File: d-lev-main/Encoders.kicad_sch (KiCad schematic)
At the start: 8 parts, among them SW1 RotaryEncoder_Switch, SW2 RotaryEncoder_Switch, SW3 RotaryEncoder_Switch, SW4 RotaryEncoder_Switch, SW5 RotaryEncoder_Switch, SW6 RotaryEncoder_Switch, SW7 RotaryEncoder_Switch, SW8 RotaryEncoder_Switch

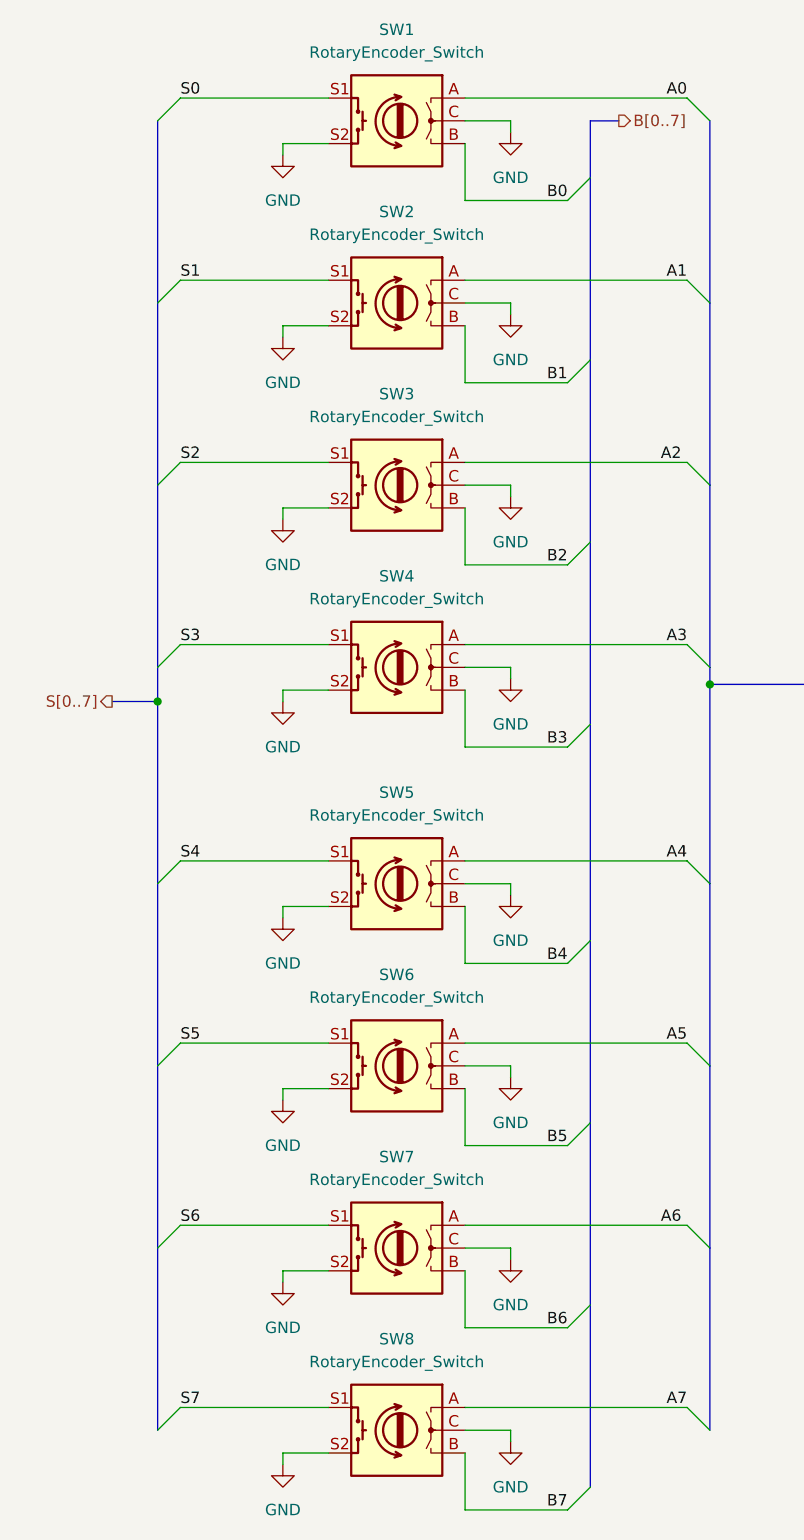
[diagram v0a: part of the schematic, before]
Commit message: Add block diagram
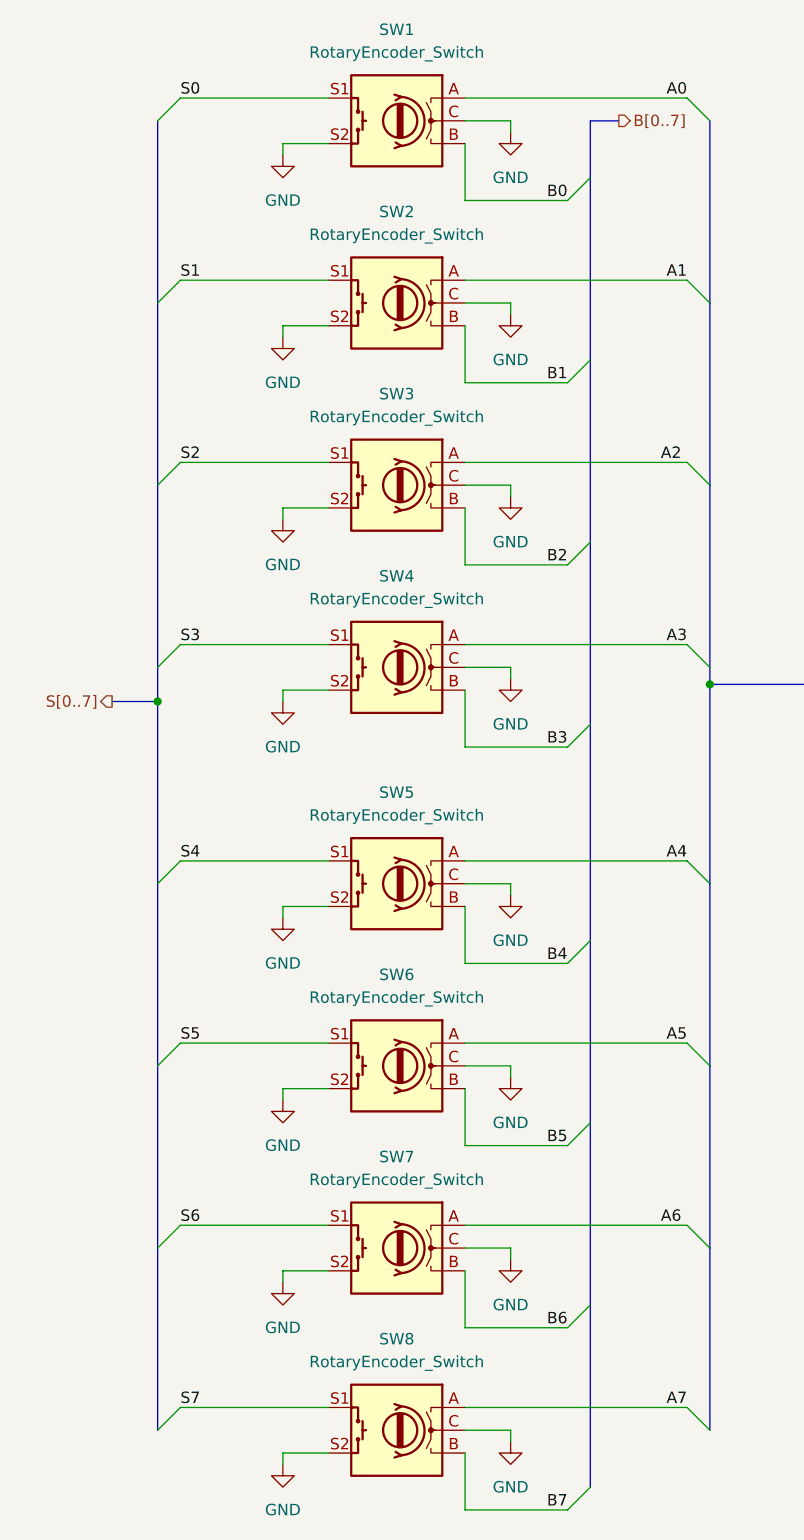
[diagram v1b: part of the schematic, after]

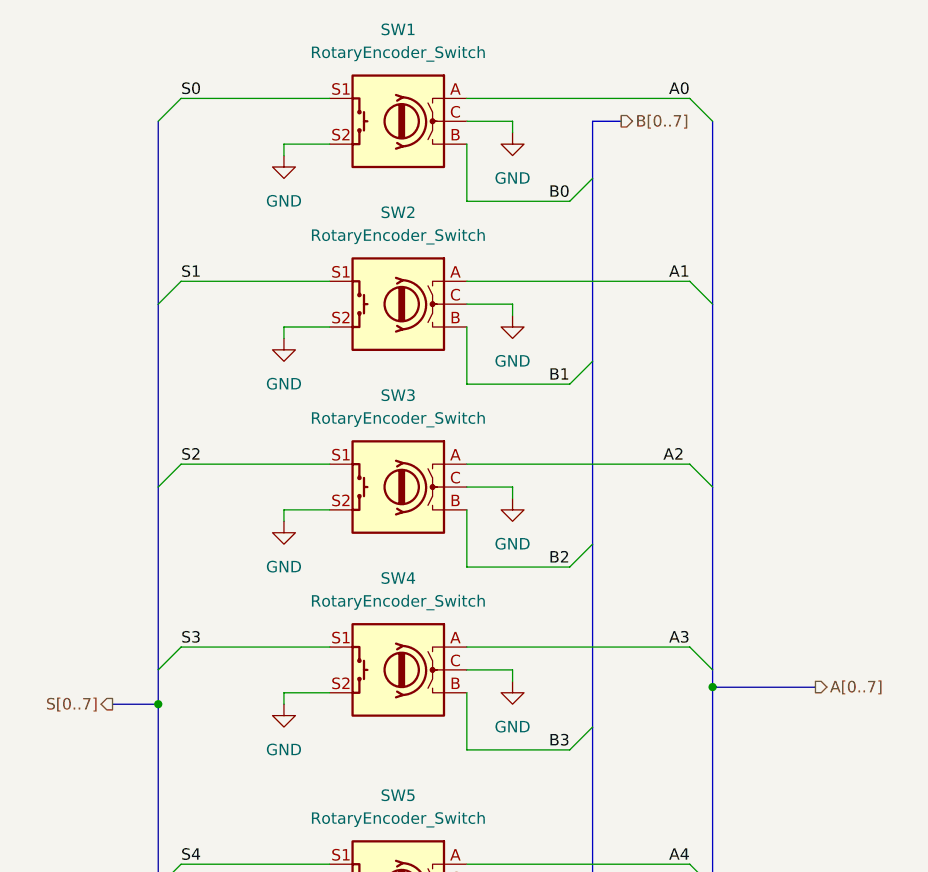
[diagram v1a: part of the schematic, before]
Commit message: Many changes
Reorganized libraries to share between projects
Set up JLC 2- and 4- layer design rules
Finished copying over most of the schematic (excluding I/O board)
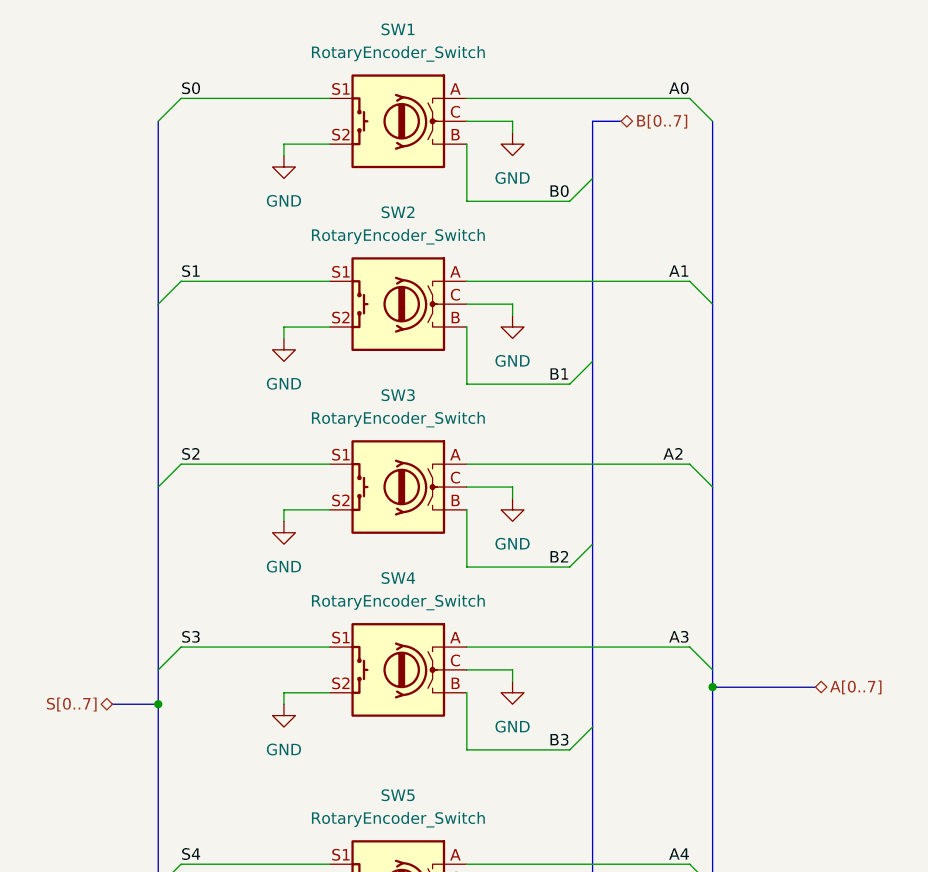
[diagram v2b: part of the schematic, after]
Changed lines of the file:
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@@
     (effects (font (size 1.27 1.27)) (justify right bottom))
   )
-  (hierarchical_label "B[0..7]" (shape output) (at 97.155 25.4 0) (fields_autoplaced)
+  (hierarchical_label "B[0..7]" (shape bidirectional) (at 97.155 25.4 0) (fields_autoplaced)
     (effects (font (size 1.27 1.27)) (justify left))
   )
-  (hierarchical_label "S[0..7]" (shape output) (at 40.64 90.17 180) (fields_autoplaced)
+  (hierarchical_label "S[0..7]" (shape bidirectional) (at 40.64 90.17 180) (fields_autoplaced)
     (effects (font (size 1.27 1.27)) (justify right))
   )
-  (hierarchical_label "A[0..7]" (shape output) (at 118.745 88.265 0) (fields_autoplaced)
+  (hierarchical_label "A[0..7]" (shape bidirectional) (at 118.745 88.265 0) (fields_autoplaced)
     (effects (font (size 1.27 1.27)) (justify left))
   )
   (symbol (lib_id "power:GND") (at 59.69 175.26 0) (unit 1)
     (in_bom yes) (on_board yes) (dnp no) (fields_autoplaced)
-    (property "Reference" "#PWR0123" (at 59.69 181.61 0)
+    (property "Reference" "#PWR029" (at 59.69 181.61 0)
       (effects (font (size 1.27 1.27)) hide)
     )
@@
       (project "dlev-mini"
         (path "/eb5e8bfd-9871-4528-bf57-58851bf63907/a7ad5bc5-58e2-407c-aeb8-75270556c3dc"
-          (reference "#PWR0123") (unit 1)
+          (reference "#PWR029") (unit 1)
         )
       )
@@
   (symbol (lib_id "power:GND") (at 59.69 154.94 0) (unit 1)
     (in_bom yes) (on_board yes) (dnp no) (fields_autoplaced)
-    (property "Reference" "#PWR0124" (at 59.69 161.29 0)
+    (property "Reference" "#PWR028" (at 59.69 161.29 0)
       (effects (font (size 1.27 1.27)) hide)
     )
@@
       (project "dlev-mini"
         (path "/eb5e8bfd-9871-4528-bf57-58851bf63907/a7ad5bc5-58e2-407c-aeb8-75270556c3dc"
-          (reference "#PWR0124") (unit 1)
+          (reference "#PWR028") (unit 1)
         )
       )
@@
   (symbol (lib_id "power:GND") (at 85.09 87.63 0) (mirror y) (unit 1)
     (in_bom yes) (on_board yes) (dnp no) (fields_autoplaced)
-    (property "Reference" "#PWR0134" (at 85.09 93.98 0)
+    (property "Reference" "#PWR033" (at 85.09 93.98 0)
       (effects (font (size 1.27 1.27)) hide)
     )
@@
       (project "dlev-mini"
         (path "/eb5e8bfd-9871-4528-bf57-58851bf63907/a7ad5bc5-58e2-407c-aeb8-75270556c3dc"
-          (reference "#PWR0134") (unit 1)
+          (reference "#PWR033") (unit 1)
         )
       )
@@
   (symbol (lib_id "power:GND") (at 59.69 69.85 0) (unit 1)
     (in_bom yes) (on_board yes) (dnp no) (fields_autoplaced)
-    (property "Reference" "#PWR0135" (at 59.69 76.2 0)
+    (property "Reference" "#PWR024" (at 59.69 76.2 0)
       (effects (font (size 1.27 1.27)) hide)
     )
@@
       (project "dlev-mini"
         (path "/eb5e8bfd-9871-4528-bf57-58851bf63907/a7ad5bc5-58e2-407c-aeb8-75270556c3dc"
-          (reference "#PWR0135") (unit 1)
+          (reference "#PWR024") (unit 1)
         )
       )
@@
   (symbol (lib_id "power:GND") (at 59.69 49.53 0) (unit 1)
     (in_bom yes) (on_board yes) (dnp no) (fields_autoplaced)
-    (property "Reference" "#PWR0136" (at 59.69 55.88 0)
+    (property "Reference" "#PWR023" (at 59.69 55.88 0)
       (effects (font (size 1.27 1.27)) hide)
     )
@@
       (project "dlev-mini"
         (path "/eb5e8bfd-9871-4528-bf57-58851bf63907/a7ad5bc5-58e2-407c-aeb8-75270556c3dc"
-          (reference "#PWR0136") (unit 1)
+          (reference "#PWR023") (unit 1)
         )
       )
@@
   (symbol (lib_id "power:GND") (at 59.69 90.17 0) (unit 1)
     (in_bom yes) (on_board yes) (dnp no) (fields_autoplaced)
-    (property "Reference" "#PWR0133" (at 59.69 96.52 0)
+    (property "Reference" "#PWR025" (at 59.69 96.52 0)
       (effects (font (size 1.27 1.27)) hide)
     )
@@
       (project "dlev-mini"
         (path "/eb5e8bfd-9871-4528-bf57-58851bf63907/a7ad5bc5-58e2-407c-aeb8-75270556c3dc"
-          (reference "#PWR0133") (unit 1)
+          (reference "#PWR025") (unit 1)
         )
       )
@@
   (symbol (lib_id "power:GND") (at 85.09 46.99 0) (mirror y) (unit 1)
     (in_bom yes) (on_board yes) (dnp no) (fields_autoplaced)
-    (property "Reference" "#PWR0132" (at 85.09 53.34 0)
+    (property "Reference" "#PWR031" (at 85.09 53.34 0)
       (effects (font (size 1.27 1.27)) hide)
     )
@@
       (project "dlev-mini"
         (path "/eb5e8bfd-9871-4528-bf57-58851bf63907/a7ad5bc5-58e2-407c-aeb8-75270556c3dc"
-          (reference "#PWR0132") (unit 1)
+          (reference "#PWR031") (unit 1)
         )
       )
@@
   (symbol (lib_id "power:GND") (at 59.69 29.21 0) (unit 1)
     (in_bom yes) (on_board yes) (dnp no) (fields_autoplaced)
-    (property "Reference" "#PWR0137" (at 59.69 35.56 0)
+    (property "Reference" "#PWR022" (at 59.69 35.56 0)
       (effects (font (size 1.27 1.27)) hide)
     )
@@
       (project "dlev-mini"
         (path "/eb5e8bfd-9871-4528-bf57-58851bf63907/a7ad5bc5-58e2-407c-aeb8-75270556c3dc"
-          (reference "#PWR0137") (unit 1)
+          (reference "#PWR022") (unit 1)
         )
       )
@@
   (symbol (lib_id "power:GND") (at 59.69 114.3 0) (unit 1)
     (in_bom yes) (on_board yes) (dnp no) (fields_autoplaced)
-    (property "Reference" "#PWR0126" (at 59.69 120.65 0)
+    (property "Reference" "#PWR026" (at 59.69 120.65 0)
       (effects (font (size 1.27 1.27)) hide)
     )
@@
       (project "dlev-mini"
         (path "/eb5e8bfd-9871-4528-bf57-58851bf63907/a7ad5bc5-58e2-407c-aeb8-75270556c3dc"
-          (reference "#PWR0126") (unit 1)
+          (reference "#PWR026") (unit 1)
         )
       )
@@
   (symbol (lib_id "power:GND") (at 59.69 134.62 0) (unit 1)
     (in_bom yes) (on_board yes) (dnp no) (fields_autoplaced)
-    (property "Reference" "#PWR0122" (at 59.69 140.97 0)
+    (property "Reference" "#PWR027" (at 59.69 140.97 0)
       (effects (font (size 1.27 1.27)) hide)
     )
@@
       (project "dlev-mini"
         (path "/eb5e8bfd-9871-4528-bf57-58851bf63907/a7ad5bc5-58e2-407c-aeb8-75270556c3dc"
-          (reference "#PWR0122") (unit 1)
+          (reference "#PWR027") (unit 1)
         )
       )
@@
   (symbol (lib_id "power:GND") (at 85.09 152.4 0) (mirror y) (unit 1)
     (in_bom yes) (on_board yes) (dnp no) (fields_autoplaced)
-    (property "Reference" "#PWR0127" (at 85.09 158.75 0)
+    (property "Reference" "#PWR036" (at 85.09 158.75 0)
       (effects (font (size 1.27 1.27)) hide)
     )
@@
       (project "dlev-mini"
         (path "/eb5e8bfd-9871-4528-bf57-58851bf63907/a7ad5bc5-58e2-407c-aeb8-75270556c3dc"
-          (reference "#PWR0127") (unit 1)
+          (reference "#PWR036") (unit 1)
         )
       )
@@
   (symbol (lib_id "power:GND") (at 85.09 67.31 0) (mirror y) (unit 1)
     (in_bom yes) (on_board yes) (dnp no) (fields_autoplaced)
-    (property "Reference" "#PWR0130" (at 85.09 73.66 0)
+    (property "Reference" "#PWR032" (at 85.09 73.66 0)
       (effects (font (size 1.27 1.27)) hide)
     )
@@
       (project "dlev-mini"
         (path "/eb5e8bfd-9871-4528-bf57-58851bf63907/a7ad5bc5-58e2-407c-aeb8-75270556c3dc"
-          (reference "#PWR0130") (unit 1)
+          (reference "#PWR032") (unit 1)
         )
       )
@@
   (symbol (lib_id "power:GND") (at 85.09 26.67 0) (mirror y) (unit 1)
     (in_bom yes) (on_board yes) (dnp no) (fields_autoplaced)
-    (property "Reference" "#PWR0131" (at 85.09 33.02 0)
+    (property "Reference" "#PWR030" (at 85.09 33.02 0)
       (effects (font (size 1.27 1.27)) hide)
     )
@@
       (project "dlev-mini"
         (path "/eb5e8bfd-9871-4528-bf57-58851bf63907/a7ad5bc5-58e2-407c-aeb8-75270556c3dc"
-          (reference "#PWR0131") (unit 1)
+          (reference "#PWR030") (unit 1)
         )
       )
@@
   (symbol (lib_id "power:GND") (at 85.09 172.72 0) (mirror y) (unit 1)
     (in_bom yes) (on_board yes) (dnp no) (fields_autoplaced)
-    (property "Reference" "#PWR0128" (at 85.09 179.07 0)
+    (property "Reference" "#PWR037" (at 85.09 179.07 0)
       (effects (font (size 1.27 1.27)) hide)
     )
@@
       (project "dlev-mini"
         (path "/eb5e8bfd-9871-4528-bf57-58851bf63907/a7ad5bc5-58e2-407c-aeb8-75270556c3dc"
-          (reference "#PWR0128") (unit 1)
+          (reference "#PWR037") (unit 1)
         )
       )
@@
   (symbol (lib_id "power:GND") (at 85.09 111.76 0) (mirror y) (unit 1)
     (in_bom yes) (on_board yes) (dnp no) (fields_autoplaced)
-    (property "Reference" "#PWR0125" (at 85.09 118.11 0)
+    (property "Reference" "#PWR034" (at 85.09 118.11 0)
       (effects (font (size 1.27 1.27)) hide)
     )
@@
       (project "dlev-mini"
         (path "/eb5e8bfd-9871-4528-bf57-58851bf63907/a7ad5bc5-58e2-407c-aeb8-75270556c3dc"
-          (reference "#PWR0125") (unit 1)
+          (reference "#PWR034") (unit 1)
         )
       )
@@
   (symbol (lib_id "power:GND") (at 85.09 132.08 0) (mirror y) (unit 1)
     (in_bom yes) (on_board yes) (dnp no) (fields_autoplaced)
-    (property "Reference" "#PWR0129" (at 85.09 138.43 0)
+    (property "Reference" "#PWR035" (at 85.09 138.43 0)
       (effects (font (size 1.27 1.27)) hide)
     )
@@
       (project "dlev-mini"
         (path "/eb5e8bfd-9871-4528-bf57-58851bf63907/a7ad5bc5-58e2-407c-aeb8-75270556c3dc"
-          (reference "#PWR0129") (unit 1)
-        )
-      )
+          (reference "#PWR035") (unit 1)
+        )
+      )
